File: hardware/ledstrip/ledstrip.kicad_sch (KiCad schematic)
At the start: 18 parts, among them J1 Conn_ARM_JTAG_SWD_10, J2 USB_C_Receptacle_USB2.0_16P, U1 STM32G030K6Tx, U2 CP2102N-A02-GQFN20, U4 USBLC6-2SC6

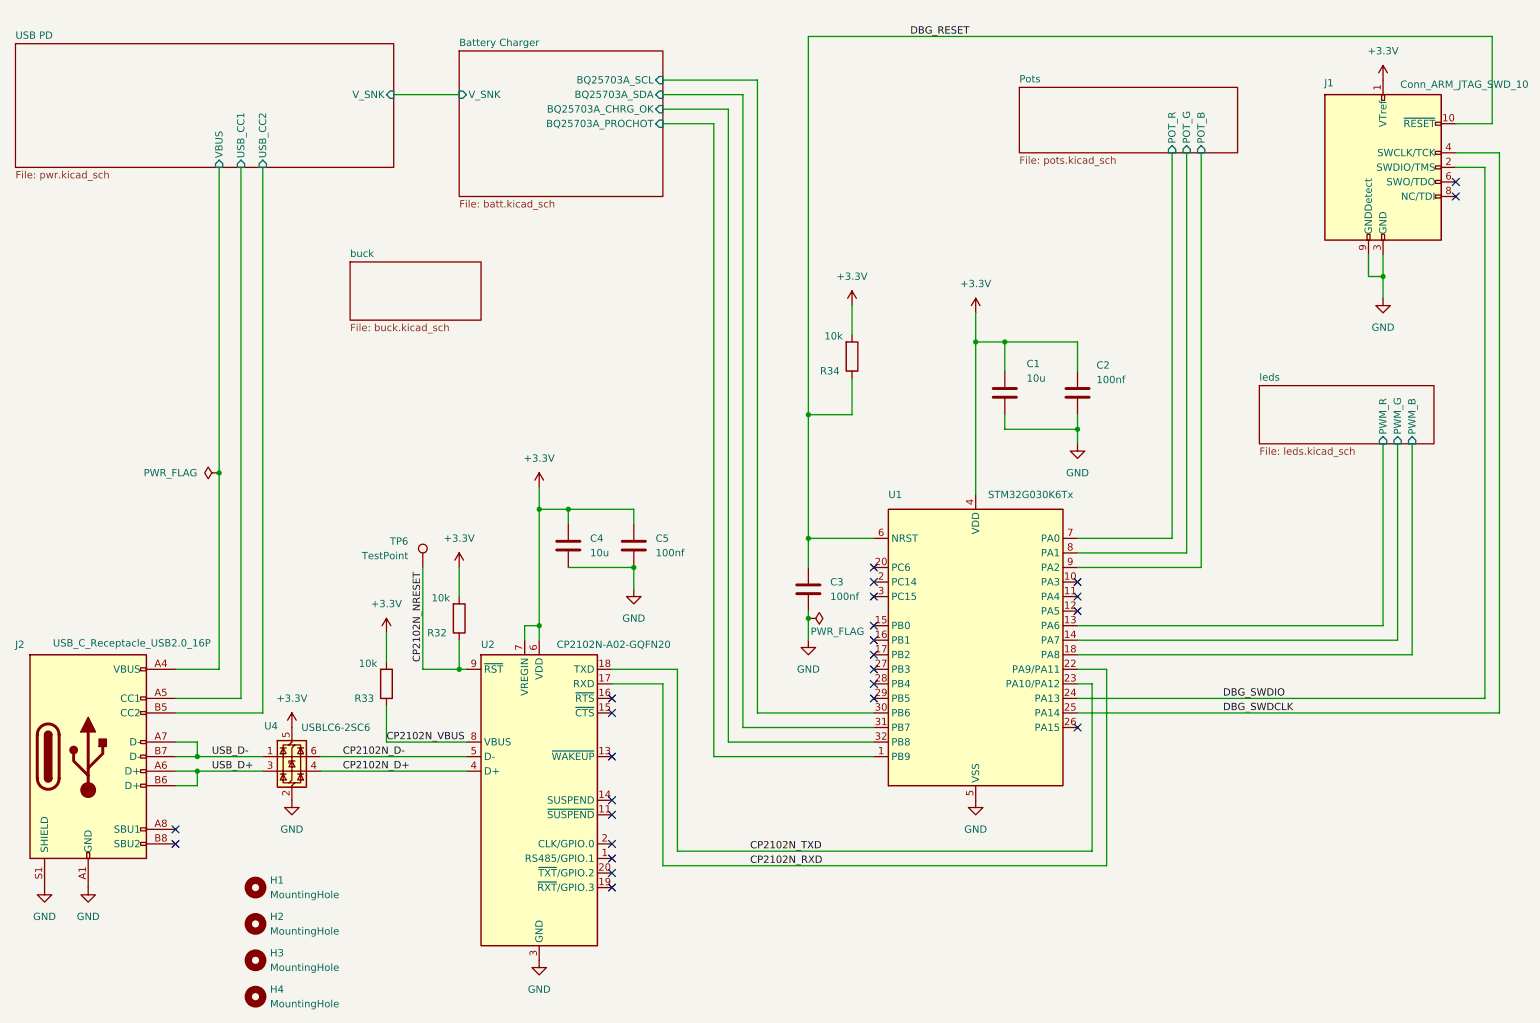
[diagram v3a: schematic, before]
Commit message: Fix ILIM_HIZ setting on BQ25703A
Add comments on schematics about hardware configuration.
Setup a early stable 2.5V from REGN to setup ILIM_HIZ correctly.
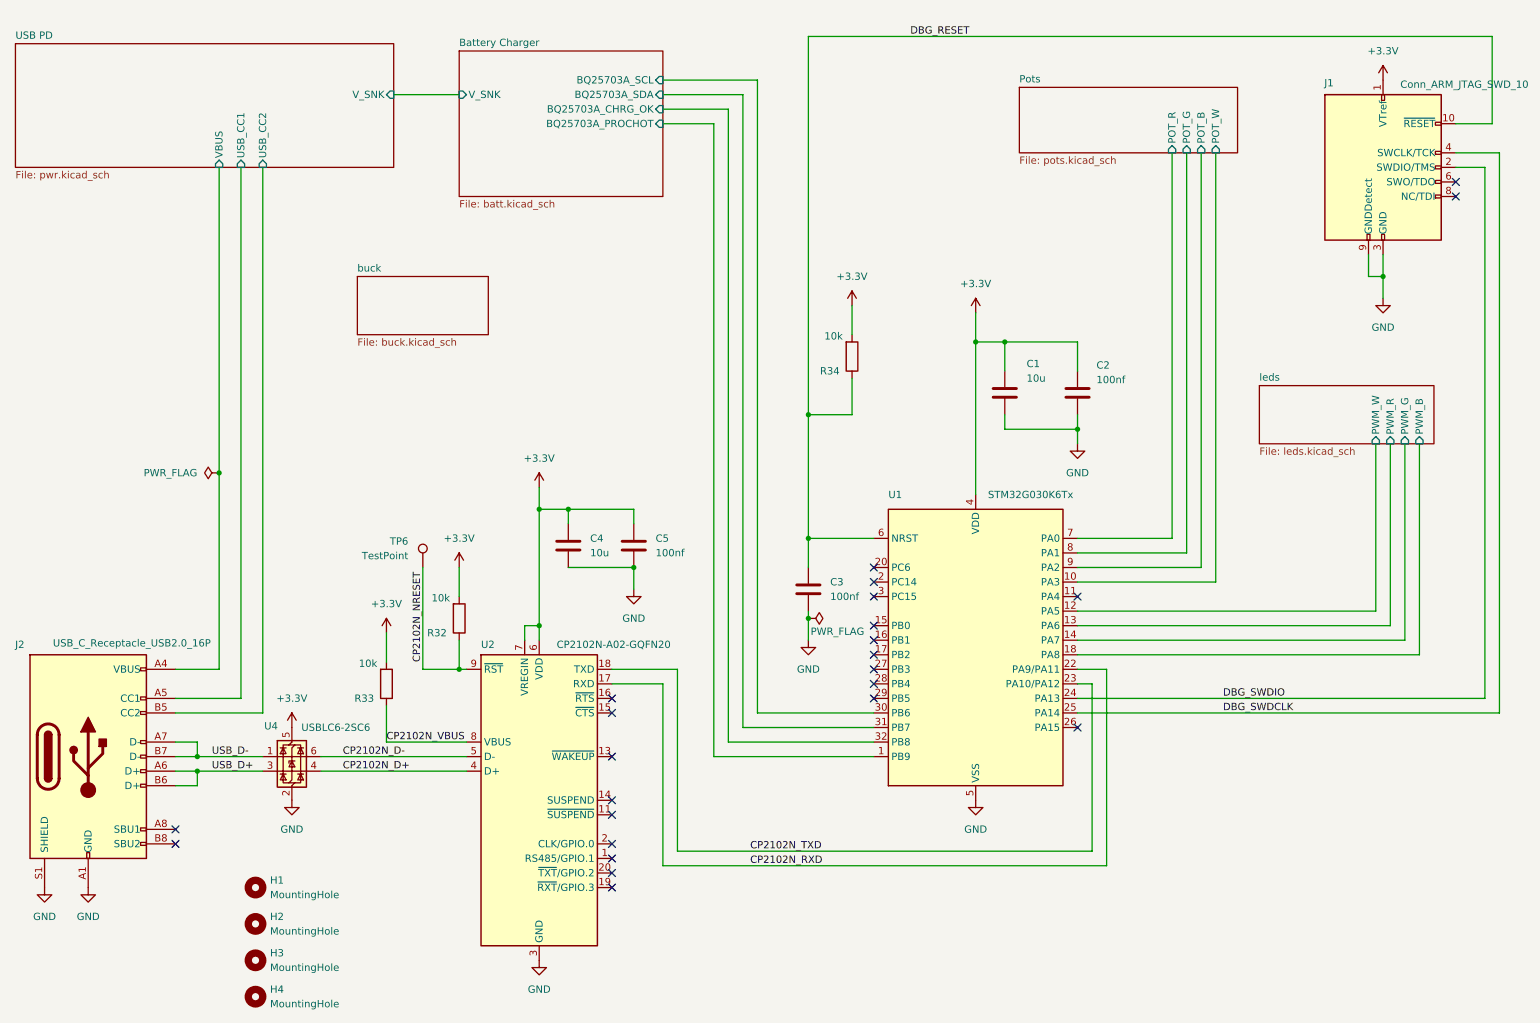
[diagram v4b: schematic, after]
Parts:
- U1: Distributor Link 2 (none) -> https://www.digikey.com/en/products/detail/stmicroelectroni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; Field8Distributor Link 1Distributor Link 2 https://www.digikey.com/en/products/detail/stmicroelectroni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 -> (none)
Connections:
- net Pots/POT_W: now reaches U1.10 (PA3)
- net leds/PWM_W: now reaches U1.12 (PA5)
- no-connect marks 26 -> 24
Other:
- sheet Pots ports: added POT_W; removed none
- sheet leds ports: added PWM_W; removed none
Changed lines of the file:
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@@
 	)
 	(no_connect
-		(at 204.47 118.11)
-	)
-	(no_connect
-		(at 204.47 113.03)
-	)
-	(no_connect
 		(at 168.91 128.27)
 	)
@@
 	(wire
 		(pts
+			(xy 228.6 38.1) (xy 228.6 113.03)
+		)
+		(stroke
+			(width 0)
+			(type default)
+		)
+	)
+	(wire
+		(pts
 			(xy 110.49 100.33) (xy 115.57 100.33)
 		)
@@
 	(wire
 		(pts
+			(xy 256.54 118.11) (xy 256.54 88.9)
+		)
+		(stroke
+			(width 0)
+			(type default)
+		)
+	)
+	(wire
+		(pts
 			(xy 257.81 59.69) (xy 257.81 55.88)
 		)
@@
 	(wire
 		(pts
+			(xy 204.47 118.11) (xy 256.54 118.11)
+		)
+		(stroke
+			(width 0)
+			(type default)
+		)
+	)
+	(wire
+		(pts
 			(xy 72.39 143.51) (xy 97.79 143.51)
 		)
@@
 	(wire
 		(pts
-			(xy 262.89 125.73) (xy 262.89 88.9)
+			(xy 264.16 125.73) (xy 264.16 88.9)
 		)
 		(stroke
@@
 	(wire
 		(pts
-			(xy 204.47 123.19) (xy 260.35 123.19)
+			(xy 204.47 123.19) (xy 261.62 123.19)
 		)
 		(stroke
@@
 	(wire
 		(pts
-			(xy 257.81 120.65) (xy 257.81 88.9)
+			(xy 259.08 120.65) (xy 259.08 88.9)
 		)
 		(stroke
@@
 	(wire
 		(pts
-			(xy 204.47 120.65) (xy 257.81 120.65)
+			(xy 204.47 120.65) (xy 259.08 120.65)
 		)
 		(stroke
@@
 	(wire
 		(pts
-			(xy 260.35 123.19) (xy 260.35 88.9)
+			(xy 261.62 123.19) (xy 261.62 88.9)
 		)
 		(stroke
@@
 	(wire
 		(pts
-			(xy 204.47 125.73) (xy 262.89 125.73)
+			(xy 204.47 125.73) (xy 264.16 125.73)
 		)
 		(stroke
@@
 		)
 	)
+	(wire
+		(pts
+			(xy 204.47 113.03) (xy 228.6 113.03)
+		)
+		(stroke
+			(width 0)
+			(type default)
+		)
+	)
 	(label "CP2102N_VBUS"
 		(at 83.82 140.97 0)
@@
 			)
 		)
-		(property "Field8Distributor Link 1Distributor Link 2" "https://www.digikey.com/en/products/detail/stmicroelectronics/STM32G030K6T6/10326688"
+		(property "Distributor Link 2" "https://www.digikey.com/en/products/detail/stmicroelectronics/STM32G030K6T6/10326688"
 			(at 186.69 125.73 0)
 			(effects
@@
 			)
 		)
+		(pin "POT_W" input
+			(at 228.6 38.1 270)
+			(effects
+				(font
+					(size 1.27 1.27)
+				)
+				(justify left)
+			)
+		)
 		(instances
 			(project "ledstrip"
@@
 	)
 	(sheet
-		(at 77.47 57.15)
+		(at 78.74 59.69)
 		(size 22.86 10.16)
 		(exclude_from_sim no)
@@
 		)
 		(property "Sheetname" "buck"
-			(at 77.47 56.4384 0)
+			(at 78.74 58.9784 0)
 			(effects
 				(font
@@
 		)
 		(property "Sheetfile" "buck.kicad_sch"
-			(at 77.47 67.8946 0)
+			(at 78.74 70.4346 0)
 			(effects
 				(font
@@
 		)
 		(pin "PWM_B" input
-			(at 262.89 88.9 270)
+			(at 264.16 88.9 270)
 			(effects
 				(font
@@
 		)
 		(pin "PWM_G" input
-			(at 260.35 88.9 270)
+			(at 261.62 88.9 270)
 			(effects
 				(font
@@
 		)
 		(pin "PWM_R" input
-			(at 257.81 88.9 270)
+			(at 259.08 88.9 270)
+			(effects
+				(font
+					(size 1.27 1.27)
+				)
+				(justify left)
+			)
+		)
+		(pin "PWM_W" input
+			(at 256.54 88.9 270)
 			(effects
 				(font

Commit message: Wire STUSB4500 I2C to MCU
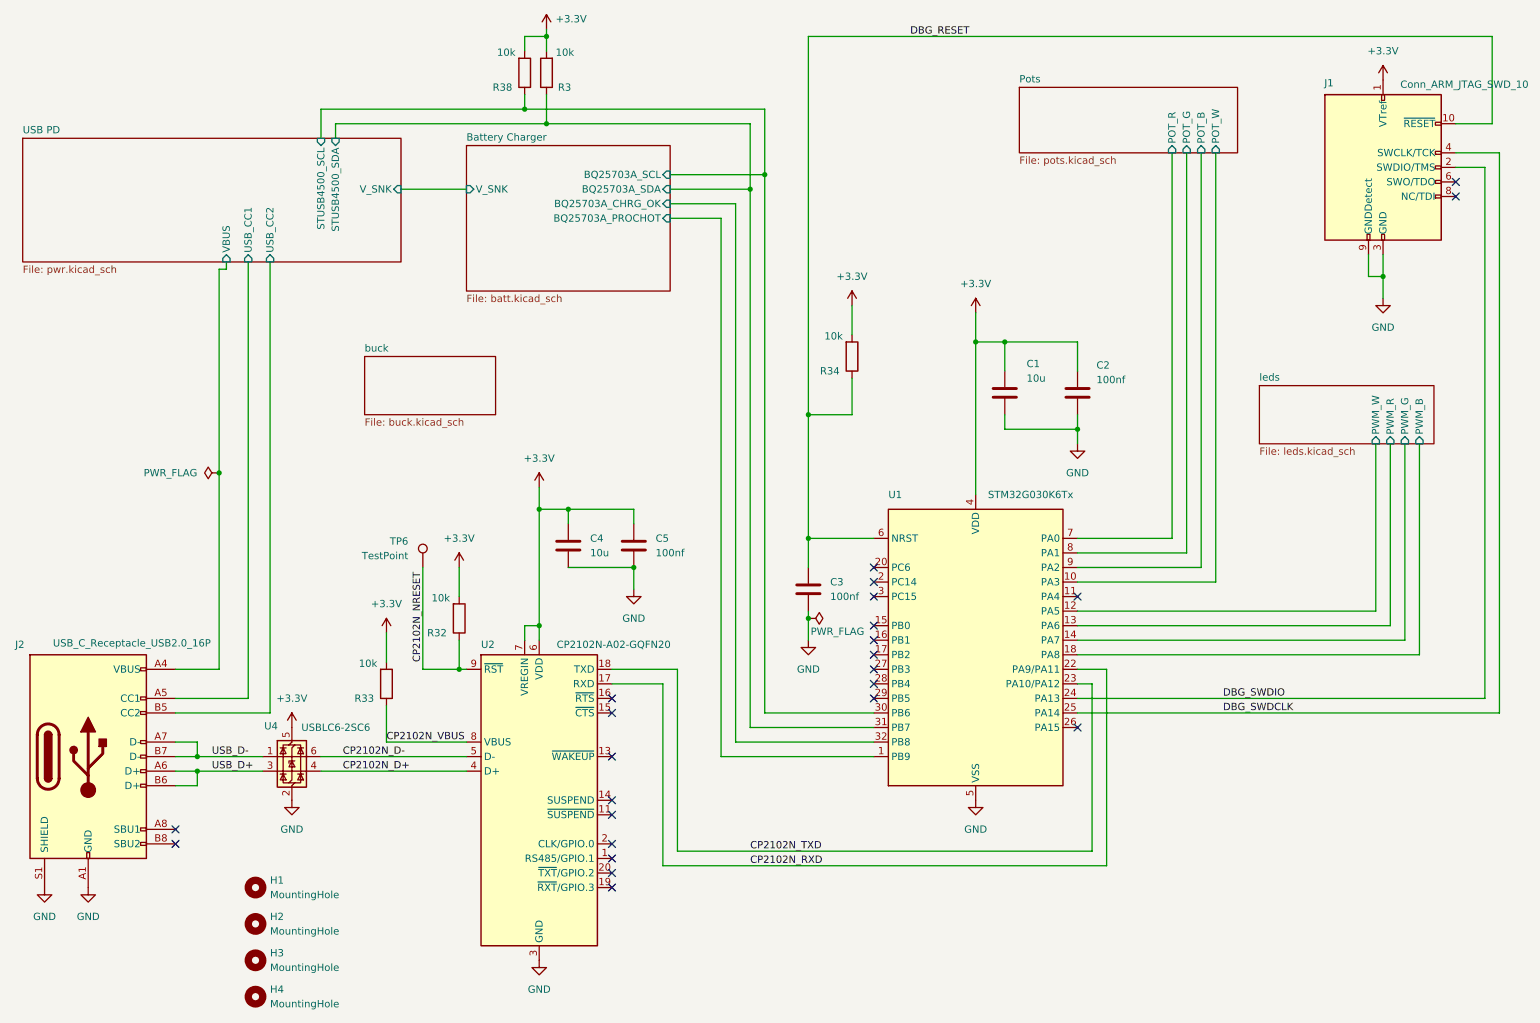
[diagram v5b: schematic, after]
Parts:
- added R3, R38: 10k, Resistor_SMD:R_0805_2012Metric, symbol Device:R
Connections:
- net +3.3V: now also R3.2, R38.2
- net Battery Charger/BQ25703A_SCL: now also R38.1
- net Battery Charger/BQ25703A_SDA: now also R3.1
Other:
- sheet USB PD ports: added STUSB4500_SCL, STUSB4500_SDA; removed none

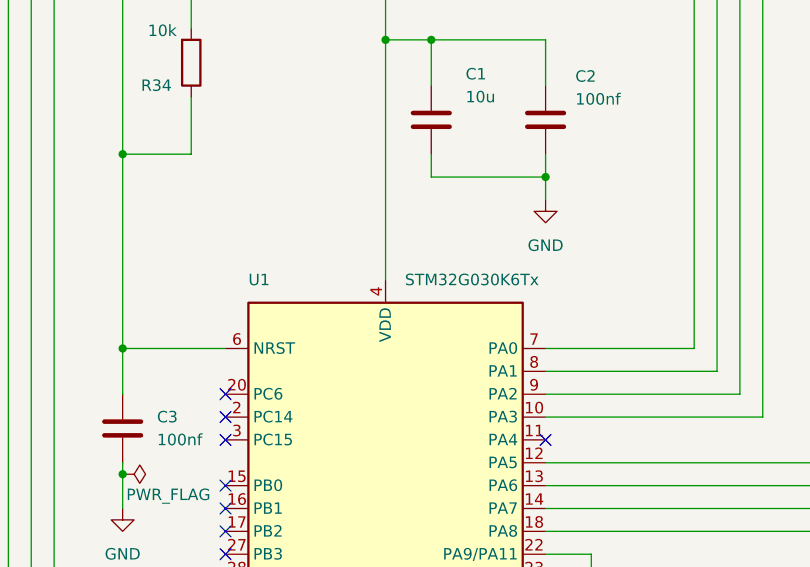
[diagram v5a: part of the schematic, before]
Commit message: Added GND zone in L2 layer + vias for ground.
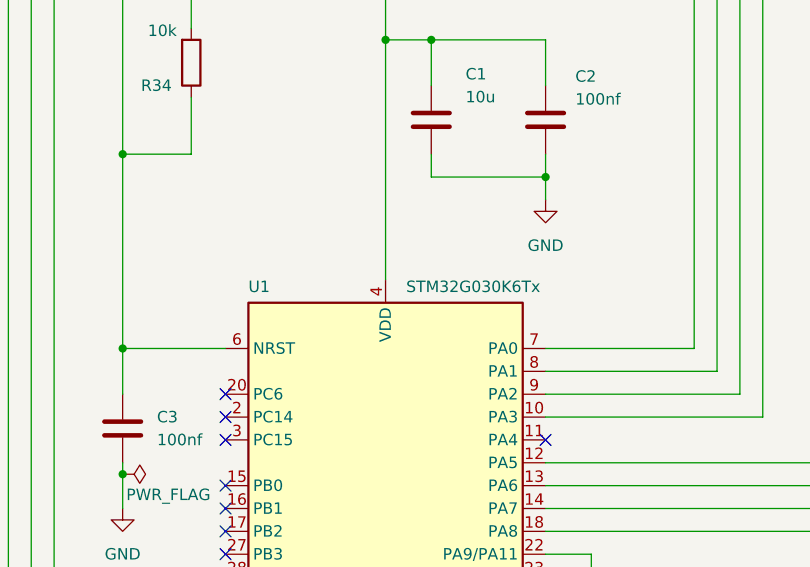
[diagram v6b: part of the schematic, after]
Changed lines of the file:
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@@
 		(dnp no)
 		(property "Reference" "U1"
-			(at 171.45 97.79 0)
+			(at 171.45 98.552 0)
 			(effects
 				(font
@@
 		)
 		(property "Value" "STM32G030K6Tx"
-			(at 188.8333 97.79 0)
+			(at 188.976 98.552 0)
 			(effects
 				(font

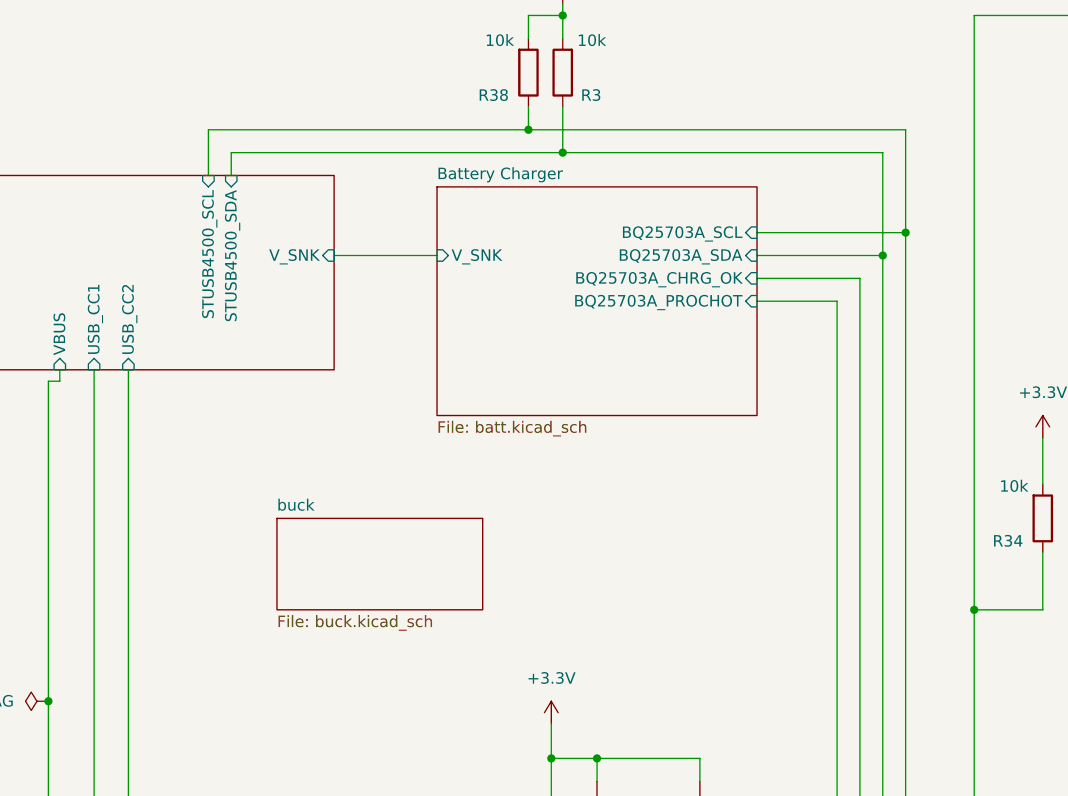
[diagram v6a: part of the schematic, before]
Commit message: Add ON/OFF button to PCB.
Decrease power zone size.
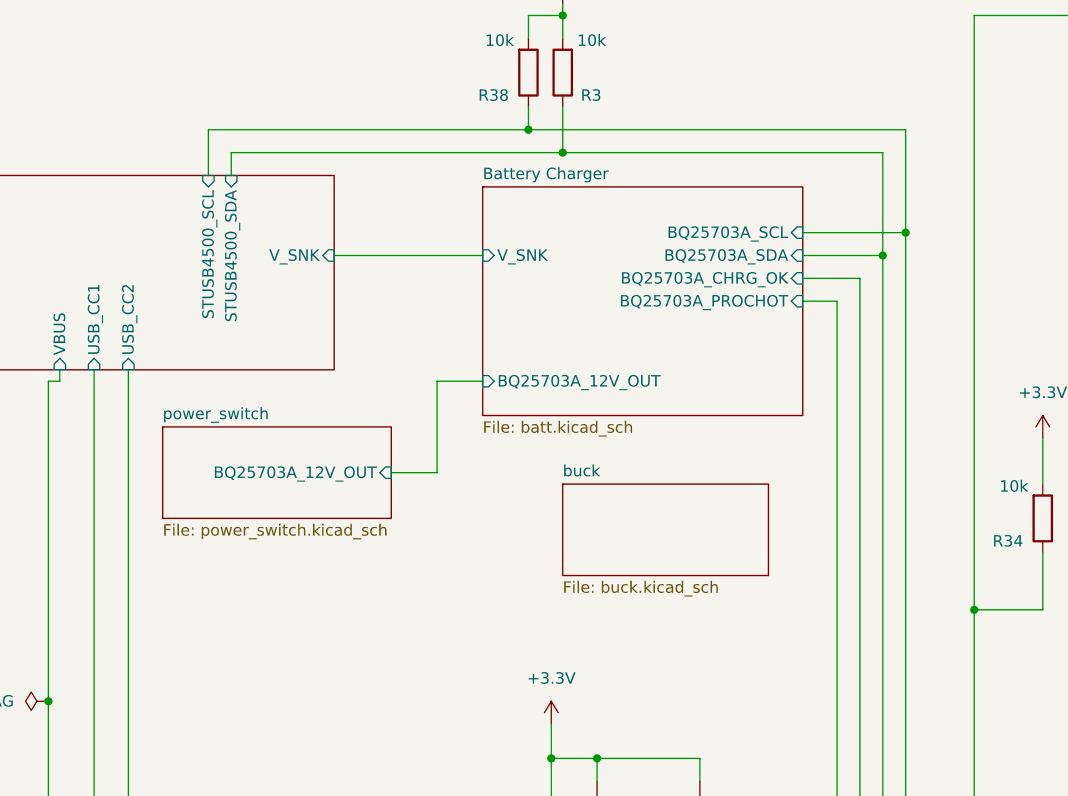
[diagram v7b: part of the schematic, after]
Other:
- added sheet power_switch (power_switch.kicad_sch)
- sheet Battery Charger ports: added BQ25703A_12V_OUT; removed none
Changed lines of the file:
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@@
 	(wire
 		(pts
+			(xy 92.71 68.58) (xy 97.79 68.58)
+		)
+		(stroke
+			(width 0)
+			(type default)
+		)
+	)
+	(wire
+		(pts
 			(xy 46.99 146.05) (xy 50.8 146.05)
 		)
@@
 	(wire
 		(pts
-			(xy 86.36 44.45) (xy 97.79 44.45)
+			(xy 86.36 44.45) (xy 102.87 44.45)
 		)
 		(stroke
@@
 	(wire
 		(pts
+			(xy 97.79 58.42) (xy 102.87 58.42)
+		)
+		(stroke
+			(width 0)
+			(type default)
+		)
+	)
+	(wire
+		(pts
 			(xy 270.51 38.1) (xy 278.13 38.1)
 		)
@@
 	(wire
 		(pts
-			(xy 133.35 44.45) (xy 147.32 44.45)
+			(xy 138.43 44.45) (xy 147.32 44.45)
 		)
 		(stroke
@@
 	(wire
 		(pts
-			(xy 142.24 49.53) (xy 133.35 49.53)
+			(xy 142.24 49.53) (xy 138.43 49.53)
 		)
 		(stroke
@@
 	(wire
 		(pts
+			(xy 97.79 68.58) (xy 97.79 58.42)
+		)
+		(stroke
+			(width 0)
+			(type default)
+		)
+	)
+	(wire
+		(pts
 			(xy 123.19 128.27) (xy 134.62 128.27)
 		)
@@
 	(wire
 		(pts
-			(xy 133.35 46.99) (xy 144.78 46.99)
+			(xy 138.43 46.99) (xy 144.78 46.99)
 		)
 		(stroke
@@
 	(wire
 		(pts
-			(xy 133.35 41.91) (xy 149.86 41.91)
+			(xy 138.43 41.91) (xy 149.86 41.91)
 		)
 		(stroke
@@
 	)
 	(sheet
-		(at 80.01 73.66)
+		(at 111.76 69.85)
 		(size 22.86 10.16)
 		(exclude_from_sim no)
@@
 		)
 		(property "Sheetname" "buck"
-			(at 80.01 72.9484 0)
+			(at 111.76 69.1384 0)
 			(effects
 				(font
@@
 		)
 		(property "Sheetfile" "buck.kicad_sch"
-			(at 80.01 84.4046 0)
+			(at 111.76 80.5946 0)
 			(effects
 				(font
@@
 	)
 	(sheet
-		(at 97.79 36.83)
+		(at 102.87 36.83)
 		(size 35.56 25.4)
 		(exclude_from_sim no)
@@
 		)
 		(property "Sheetname" "Battery Charger"
-			(at 97.79 36.1184 0)
+			(at 102.87 36.1184 0)
 			(effects
 				(font
@@
 		)
 		(property "Sheetfile" "batt.kicad_sch"
-			(at 97.79 62.8146 0)
+			(at 102.87 62.8146 0)
 			(effects
 				(font
@@
 		)
 		(pin "BQ25703A_SCL" input
-			(at 133.35 41.91 0)
+			(at 138.43 41.91 0)
 			(effects
 				(font
@@
 		)
 		(pin "BQ25703A_SDA" input
-			(at 133.35 44.45 0)
+			(at 138.43 44.45 0)
 			(effects
 				(font
@@
 		)
 		(pin "V_SNK" input
-			(at 97.79 44.45 180)
+			(at 102.87 44.45 180)
 			(effects
 				(font
@@
 		)
 		(pin "BQ25703A_CHRG_OK" input
-			(at 133.35 46.99 0)
+			(at 138.43 46.99 0)
 			(effects
 				(font
@@
 		)
 		(pin "BQ25703A_PROCHOT" input
-			(at 133.35 49.53 0)
+			(at 138.43 49.53 0)
 			(effects
 				(font
@@
 			)
 		)
+		(pin "BQ25703A_12V_OUT" input
+			(at 102.87 58.42 180)
+			(effects
+				(font
+					(size 1.27 1.27)
+				)
+				(justify left)
+			)
+		)
 		(instances
 			(project "ledstrip"
@@
 				)
 			)
+		)
+	)
+	(sheet
+		(at 67.31 63.5)
+		(size 25.4 10.16)
+		(exclude_from_sim no)
+		(in_bom yes)
+		(on_board yes)
+		(dnp no)
+		(fields_autoplaced yes)
+		(stroke
+			(width 0.1524)
+			(type solid)
+		)
+		(fill
+			(color 0 0 0 0.0000)
+		)
+		(property "Sheetname" "power_switch"
+			(at 67.31 62.7884 0)
+			(effects
+				(font
+					(size 1.27 1.27)
+				)
+				(justify left bottom)
+			)
+		)
+		(property "Sheetfile" "power_switch.kicad_sch"
+			(at 67.31 74.2446 0)
+			(effects
+				(font
+					(size 1.27 1.27)
+				)
+				(justify left top)
+			)
+		)
+		(pin "BQ25703A_12V_OUT" input
+			(at 92.71 68.58 0)
+			(effects
+				(font
+					(size 1.27 1.27)
+				)
+				(justify right)
+			)
+		)
+		(instances
+			(project "ledstrip"
+				(path "/dcb997ee-94c4-4df2-ba22-0e091735ddd7"
+					(page "7")
+				)
+			)
